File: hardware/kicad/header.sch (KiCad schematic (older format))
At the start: 1 part, among them CN1 ADAFRUIT_FEATHER

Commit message: bugfix
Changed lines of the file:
@@
 L power-supply:+3V3 #PWR0111
 U 1 1 5E8C9068
-P 5200 2950
-F 0 "#PWR0111" H 5200 2800 50  0001 C CNN
-F 1 "+3V3" V 5215 3078 50  0000 L CNN
-F 2 "" H 5200 2950 50  0000 C CNN
-F 3 "" H 5200 2950 50  0000 C CNN
-	1    5200 2950
-	0    -1   -1   0
+P 4550 2850
+F 0 "#PWR0111" H 4550 2700 50  0001 C CNN
+F 1 "+3V3" V 4565 2978 50  0000 L CNN
+F 2 "" H 4550 2850 50  0000 C CNN
+F 3 "" H 4550 2850 50  0000 C CNN
+	1    4550 2850
+	1    0    0    -1
 $EndComp
 $Comp
 L power-supply:GND #PWR0112
 U 1 1 5E8C92B8
-P 5200 3150
-F 0 "#PWR0112" H 5200 2900 50  0001 C CNN
-F 1 "GND" V 5205 3022 50  0000 R CNN
-F 2 "" H 5200 3150 50  0000 C CNN
-F 3 "" H 5200 3150 50  0000 C CNN
-	1    5200 3150
-	0    1    1    0
+P 4550 3200
+F 0 "#PWR0112" H 4550 2950 50  0001 C CNN
+F 1 "GND" V 4555 3072 50  0000 R CNN
+F 2 "" H 4550 3200 50  0000 C CNN
+F 3 "" H 4550 3200 50  0000 C CNN
+	1    4550 3200
+	1    0    0    -1
 $EndComp
 $Comp
 L power-supply:GND #PWR0113
 U 1 1 5E8C9498
-P 5200 4350
-F 0 "#PWR0113" H 5200 4100 50  0001 C CNN
-F 1 "GND" V 5205 4222 50  0000 R CNN
-F 2 "" H 5200 4350 50  0000 C CNN
-F 3 "" H 5200 4350 50  0000 C CNN
-	1    5200 4350
-	0    1    1    0
+P 5200 4450
+F 0 "#PWR0113" H 5200 4200 50  0001 C CNN
+F 1 "GND" V 5205 4322 50  0000 R CNN
+F 2 "" H 5200 4450 50  0000 C CNN
+F 3 "" H 5200 4450 50  0000 C CNN
+	1    5200 4450
+	1    0    0    -1
 $EndComp
 Wire Wire Line
 	5350 2850 5200 2850
-Wire Wire Line
-	5200 2950 5350 2950
-Wire Wire Line
-	5350 3150 5200 3150
 Wire Wire Line
 	5200 3250 5350 3250
@@
 Wire Wire Line
 	6550 3250 6700 3250
+Wire Wire Line
+	5200 4450 5200 4350
+Wire Wire Line
+	4550 3150 4550 3200
+Wire Wire Line
+	4550 3150 5350 3150
+Wire Wire Line
+	4550 2950 4550 2850
+Wire Wire Line
+	4550 2950 5350 2950
 $EndSCHEMATC

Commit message: finished layout
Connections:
- net SPI_SCK: now reaches CN1.11 (15/SCK)
- net SPI_MOSI: now reaches CN1.12 (16/MOSI)
- net SPI_MISO: now reaches CN1.13 (14/MISO)
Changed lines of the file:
@@
 Wire Wire Line
 	4550 2950 5350 2950
+Text GLabel 5200 3950 0    50   Input ~ 0
+SPI_MOSI
+Text GLabel 5200 4050 0    50   Output ~ 0
+SPI_MISO
+Text GLabel 5200 3850 0    50   Input ~ 0
+SPI_SCK
+Wire Wire Line
+	5200 3850 5350 3850
+Wire Wire Line
+	5350 3950 5200 3950
+Wire Wire Line
+	5350 4050 5200 4050
 $EndSCHEMATC

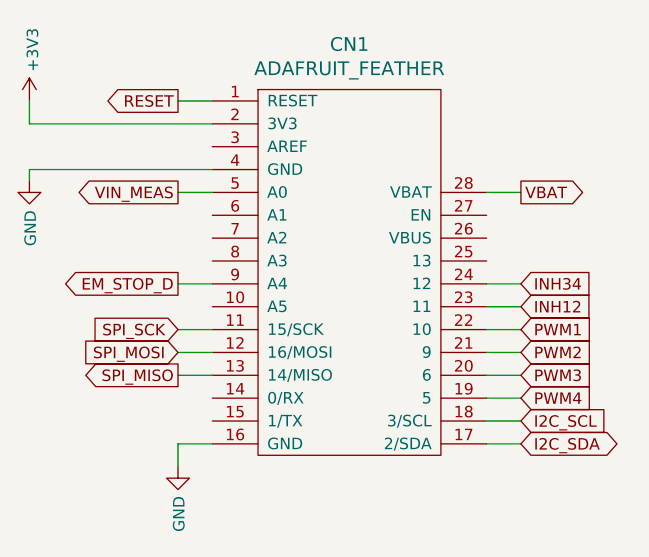
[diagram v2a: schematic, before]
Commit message: updated schematics
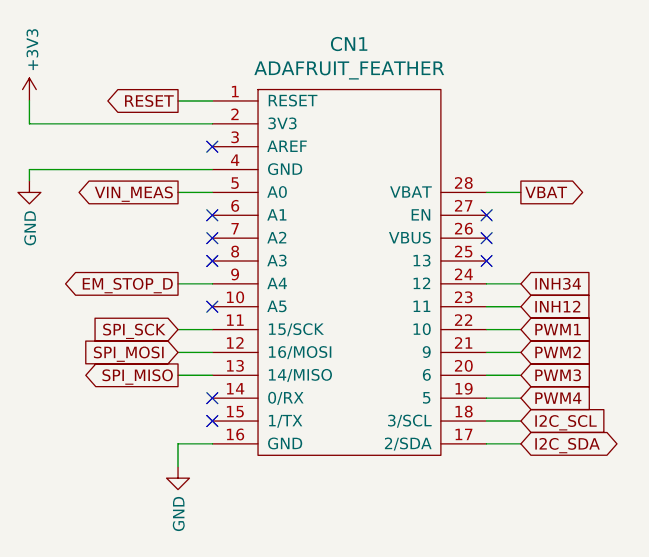
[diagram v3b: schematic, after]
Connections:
- no-connect marks 0 -> 10
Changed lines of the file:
@@
 Wire Wire Line
 	5350 4050 5200 4050
+NoConn ~ 5350 3050
+NoConn ~ 5350 3350
+NoConn ~ 5350 3450
+NoConn ~ 5350 3550
+NoConn ~ 5350 3750
+NoConn ~ 5350 4150
+NoConn ~ 5350 4250
+NoConn ~ 6550 3550
+NoConn ~ 6550 3450
+NoConn ~ 6550 3350
 $EndSCHEMATC
